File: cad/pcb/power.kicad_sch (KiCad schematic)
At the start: 39 parts, among them X1 USB_C_Receptacle_USB2.0, X2 Bat-Conn, X3 NTC-Conn

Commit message: add pcb layout
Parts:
- L2: footprint Inductor_SMD:L_0603_1608Metric -> Inductor_SMD:L_1008_2520Metric
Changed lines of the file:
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@@
       (effects (font (size 1.27 1.27)) (justify right))
     )
-    (property "Footprint" "Inductor_SMD:L_0603_1608Metric" (id 2) (at 138.43 124.46 0)
+    (property "Footprint" "Inductor_SMD:L_1008_2520Metric" (id 2) (at 138.43 124.46 0)
       (effects (font (size 1.27 1.27)) hide)
     )

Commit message: add power section on pcb layout
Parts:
- added C5: 1u, Capacitor_SMD:C_0603_1608Metric, symbol Device:C_Small
- added F1: Fuse_1A, Fuse:Fuse_0603_1608Metric_Pad1.05x0.95mm_HandSolder, symbol Device:Fuse_Small
- added FB1: FerriteBead_Small, Inductor_SMD:L_0805_2012Metric, symbol Device:FerriteBead_Small
- added TP6: Gnd, TestPoint:TestPoint_Pad_D1.0mm, symbol Connector:TestPoint
- R4: footprint Resistor_SMD:R_0603_1608Metric -> Resistor_SMD:R_2512_6332Metric
- X3: footprint Connector_JST:JST_PH_B2B-PH-SM4-TB_1x02-1MP_P2.00mm_Vertical -> myLib:PinHeader_P2mm_1x02_SMD
- renumbered C5 to C6, C6 to C7, C7 to C8, TP9 to TP10, TP6 to TP7, TP7 to TP8, TP8 to TP9
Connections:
- net BAT-: now also X2.1 (Pin_1); no longer X2.2 (Pin_2)
- net BAT_PROT+: now also X2.2 (Pin_2); no longer X2.1 (Pin_1)
- net GND: now also C5.2, TP6.1
- net VBUS: now also C5.1, FB1.2; no longer V3.1 (COMMON_A), X1.A4 (VBUS), X1.A9 (VBUS), X1.B4 (VBUS), X1.B9 (VBUS)
- new net: F1.2, FB1.1
- new net VBUS_CONN: F1.1, V3.1 (COMMON_A), X1.A4 (VBUS), X1.A9 (VBUS), X1.B4 (VBUS), X1.B9 (VBUS)

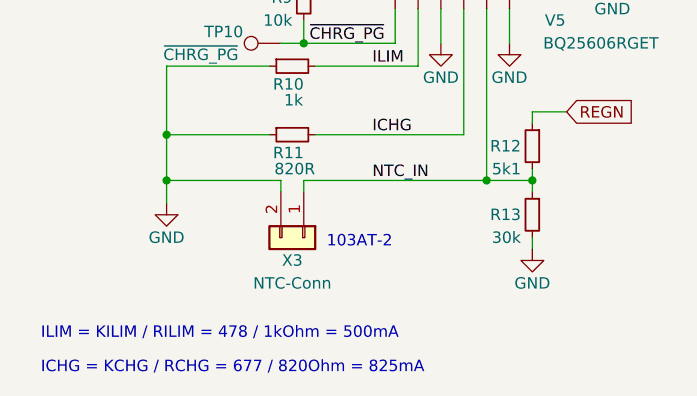
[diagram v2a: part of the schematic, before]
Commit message: add 3d models for pcb layout
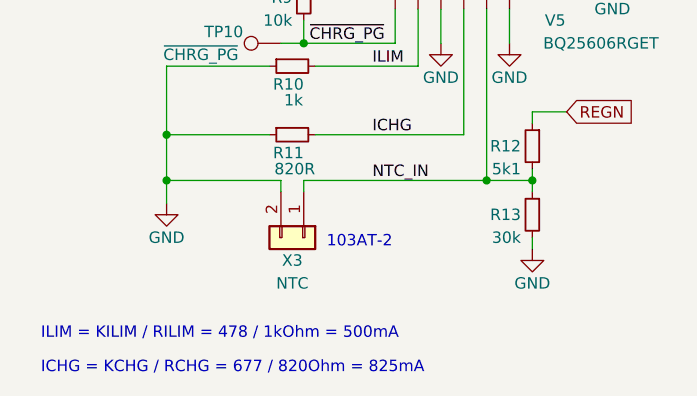
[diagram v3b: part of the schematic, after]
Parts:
- X3: value NTC-Conn -> NTC
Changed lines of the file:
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@@
     (in_bom yes) (on_board yes)
     (property "Reference" "X3" (id 0) (at 41.91 184.15 90))
-    (property "Value" "NTC-Conn" (id 1) (at 41.91 186.69 90))
+    (property "Value" "NTC" (id 1) (at 41.91 186.69 90))
     (property "Footprint" "myLib:PinHeader_P2mm_1x02_SMD" (id 2) (at 43.18 181.61 0)
       (effects (font (size 1.27 1.27)) hide)
